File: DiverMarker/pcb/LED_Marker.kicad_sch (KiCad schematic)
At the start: 27 parts, among them IC101 PIC16LF15313, J101 SKEDD6, Q100 BST-52, Q101 BST-52, SW101 MK15-C2

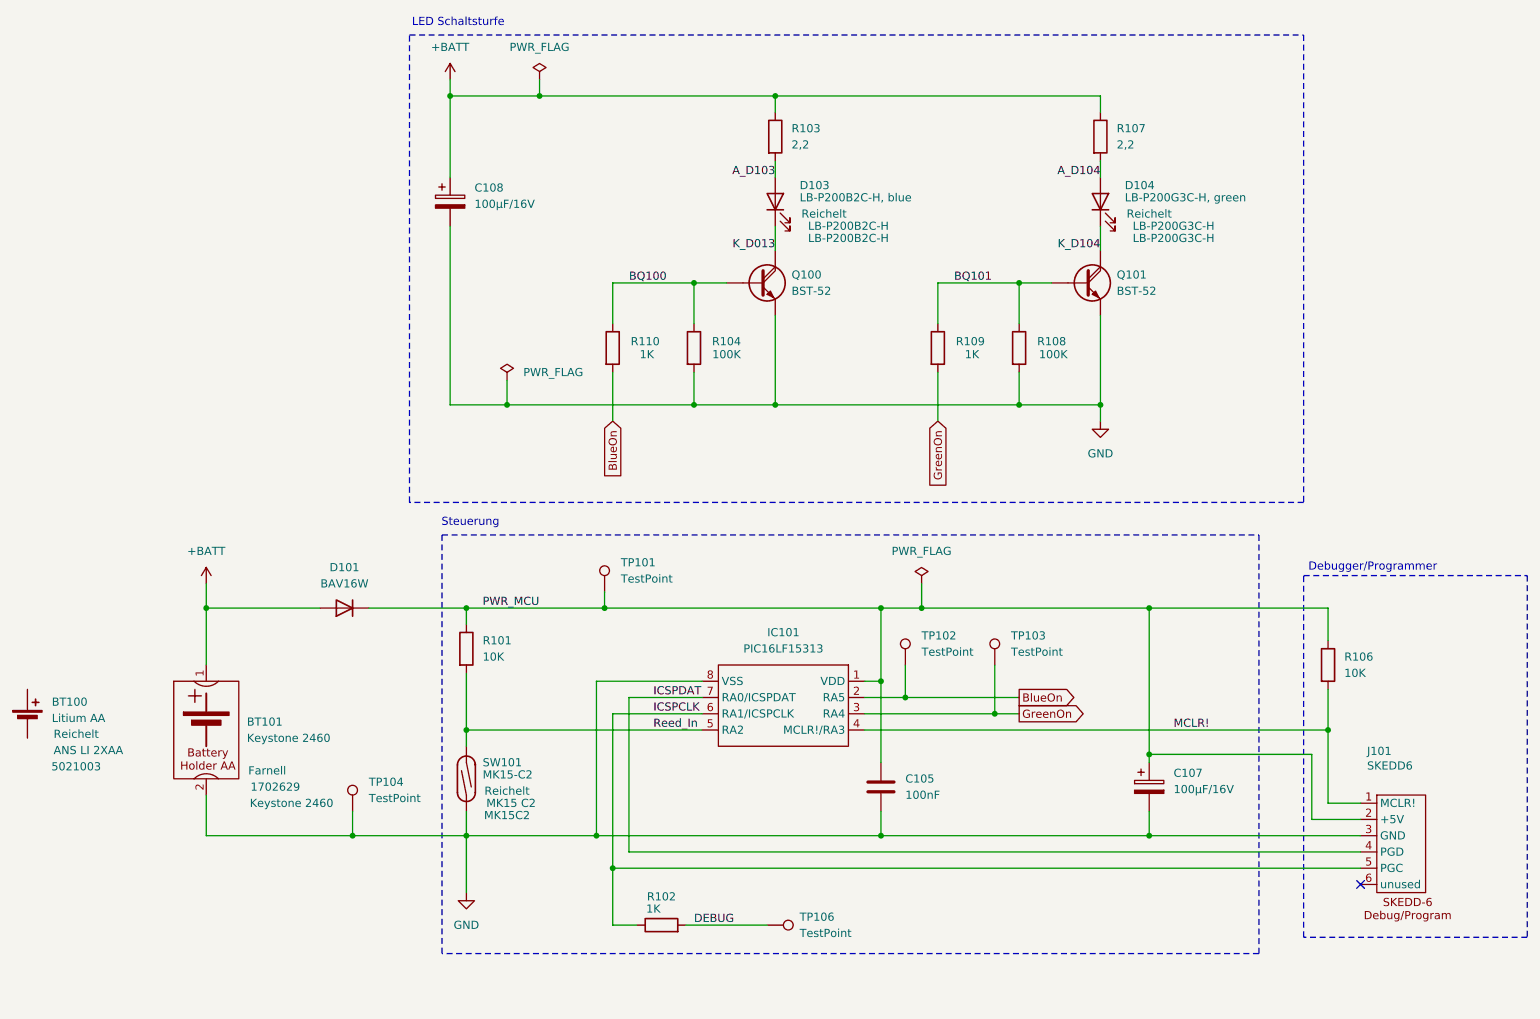
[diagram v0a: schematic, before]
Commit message: Distributors for all componentes added.
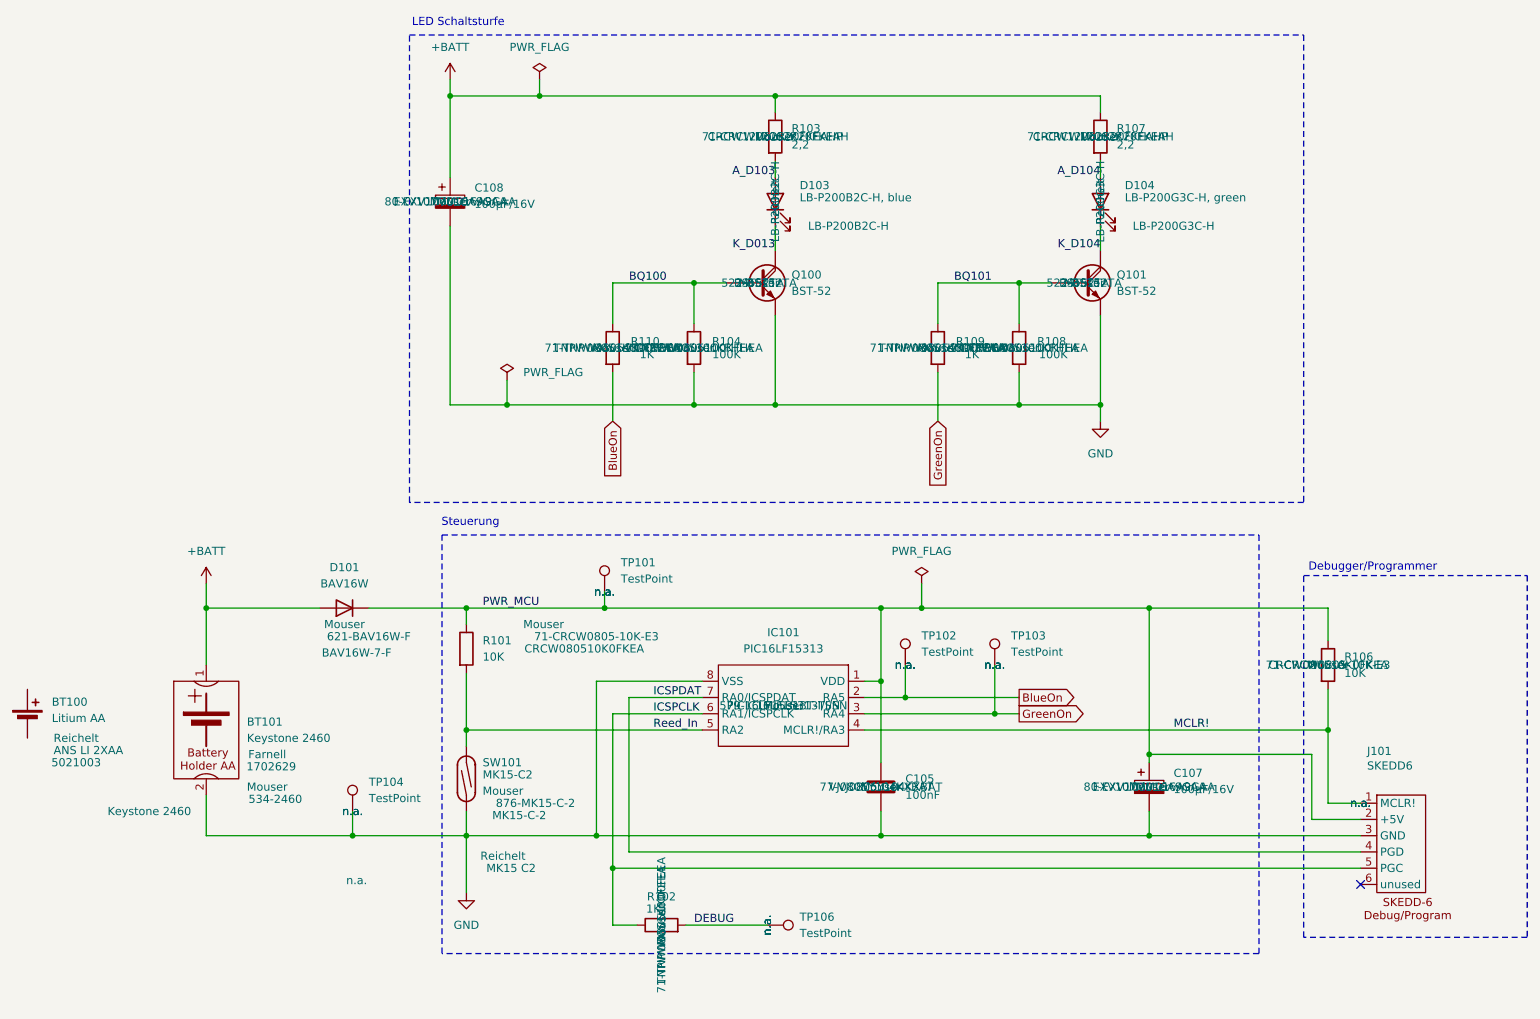
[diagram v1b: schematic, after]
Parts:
- BT100: footprint Battery:BatteryHolder_Keystone_2460_1xAA -> n.a.; Distr. Best.-Nr ANS LI 2XAA -> (none); Distr. Best.-Nr_1 (none) -> ANS LI 2XAA; Distributor Reichelt -> (none); Distributor_1 (none) -> Reichelt
- BT101: Distr. Best.-Nr 1702629 -> (none); Distr. Best.-Nr_1 (none) -> 534-2460; Distr. Best.-Nr_2 (none) -> 1702629; Distributor Farnell -> (none); Distributor_1 (none) -> Mouser; Distributor_2 (none) -> Farnell
- C105: Distr. Best.-Nr_1 (none) -> 77-VJ0805Y104KXBAT; Distributor_1 (none) -> Mouser; Herstellernummer (none) -> VJ0805Y104KXBAT
- C107, C108: Distr. Best.-Nr_1 (none) -> 80-EXV107M016A9GAA; Distributor_1 (none) -> Mouser; Herstellernummer (none) -> EXV107M016A9GAA
- D101: Distr. Best.-Nr_1 (none) -> 621-BAV16W-F; Distributor_1 (none) -> Mouser; Herstellernummer (none) -> BAV16W-7-F
- D103: Distr. Best.-Nr LB-P200B2C-H -> (none); Distr. Best.-Nr_1 (none) -> LB-P200B2C-H; Distributor Reichelt -> (none); Distributor_1 (none) -> Reichelt
- D104: Distr. Best.-Nr LB-P200G3C-H -> (none); Distr. Best.-Nr_1 (none) -> LB-P200G3C-H; Distributor Reichelt -> (none); Distributor_1 (none) -> Reichelt
- IC101: Distr. Best.-Nr_1 (none) -> 579-IC16LF15313TI/SN; Distributor_1 (none) -> Mouser; Herstellernummer (none) -> PIC16LF15313T-I/SN
- J101, TP101, TP102, TP103, TP104, TP106: Distr. Best.-Nr_1 (none) -> n.a.; Distributor_1 (none) -> n.a.; Herstellernummer (none) -> n.a.
- Q100, Q101: Distr. Best.-Nr_1 (none) -> 522-BST52TA; Distributor_1 (none) -> Mouser; Herstellernummer (none) -> BST52TA
- R101, R106: Distr. Best.-Nr_1 (none) -> 71-CRCW0805-10K-E3; Distributor_1 (none) -> Mouser; Herstellernummer (none) -> CRCW080510K0FKEA
- R102, R109, R110: Distr. Best.-Nr_1 (none) -> 71-TNPW08051K00FEEA; Distributor_1 (none) -> Mouser; Herstellernummer (none) -> TNPW08051K00FEEA
- R103, R107: Distr. Best.-Nr_1 (none) -> 71-CRCW12062R20FKEAH; Distributor_1 (none) -> Mouser; Herstellernummer (none) -> CRCW12062R20FKEAHP
- R104, R108: Distr. Best.-Nr_1 (none) -> 71-TNPW0805100KFHEA; Distributor_1 (none) -> Mouser; Herstellernummer (none) -> TNPW0805100KFHEA
- SW101: Distr. Best.-Nr MK15 C2 -> (none); Distr. Best.-Nr_1 (none) -> 876-MK15-C-2; Distr. Best.-Nr_2 (none) -> MK15 C2; Distributor Reichelt -> (none); Distributor_1 (none) -> Mouser; Distributor_2 (none) -> Reichelt; Herstellernummer MK15C2 -> MK15-C-2

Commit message: Working on BON
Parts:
- J101, TP101, TP102, TP103, TP104, TP106: Distributor_1 n.a. -> (none)
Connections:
- net GND: no longer C107.2, J101.3 (GND)
- new net: C107.2, J101.3 (GND)

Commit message: Minor changes: - LED blue replaced by red one (curret is on blue too low) - LED resistors changed from 2.2Ohm to 1Ohm - quiescent current added (about 25µA)
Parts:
- removed D103: LB-P200B2C-H, blue, MyLED:LPB200XX, symbol Device:LED
- added D105: LB-P200R1C-H, red, MyLED:LPB200XX, symbol Device:LED
- R103, R107: value 2,2 -> 1; Distr. Best.-Nr_1 71-CRCW12062R20FKEAH -> 71-CRCW12061R00FKEAH; Herstellernummer CRCW12062R20FKEAHP -> CRCW12061R00FKEAHP
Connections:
- net A_D103: now also D105.2 (A)
- net K_D013: now also D105.1 (K)

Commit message: Table with current measurements added.
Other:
- note added: "LED-Strom ca. 100mA"
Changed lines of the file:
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@@
 	)
 	(rectangle
-		(start 87.63 96.52)
-		(end 215.265 161.925)
+		(start 86.36 100.33)
+		(end 213.995 165.735)
 		(stroke
 			(width 0)
@@
 		)
 	)
+	(text "LED-Strom ca. 100mA"
+		(exclude_from_sim no)
+		(at 165.608 38.608 0)
+		(effects
+			(font
+				(size 1.27 1.27)
+			)
+		)
+	)
 	(text "LED Schaltsturfe\n"
 		(exclude_from_sim no)
@@
 		)
 	)
+	(table
+		(column_count 3)
+		(border
+			(external yes)
+			(header yes)
+			(stroke
+				(width 0)
+				(type solid)
+			)
+		)
+		(separators
+			(rows yes)
+			(cols yes)
+			(stroke
+				(width 0)
+				(type solid)
+			)
+		)
+		(column_widths 19.05 19.05 19.05)
+		(row_heights 2.54 2.54 2.54)
+		(cells
+			(table_cell ""
+				(exclude_from_sim no)
+				(at 226.06 17.78 0)
+				(size 19.05 2.54)
+				(margins 0.9525 0.9525 0.9525 0.9525)
+				(span 1 1)
+				(fill
+					(type none)
+				)
+				(effects
+					(font
+						(size 1.27 1.27)
+					)
+					(justify left top)
+				)
+			)
+			(table_cell "LED rot"
+				(exclude_from_sim no)
+				(at 245.11 17.78 0)
+				(size 19.05 2.54)
+				(margins 0.9525 0.9525 0.9525 0.9525)
+				(span 1 1)
+				(fill
+					(type none)
+				)
+				(effects
+					(font
+						(size 1.27 1.27)
+					)
+					(justify left top)
+				)
+			)
+			(table_cell "LED grün"
+				(exclude_from_sim no)
+				(at 264.16 17.78 0)
+				(size 19.05 2.54)
+				(margins 0.9525 0.9525 0.9525 0.9525)
+				(span 1 1)
+				(fill
+					(type none)
+				)
+				(effects
+					(font
+						(size 1.27 1.27)
+					)
+					(justify left top)
+				)
+			)
+			(table_cell "Brennspannung"
+				(exclude_from_sim no)
+				(at 226.06 20.32 0)
+				(size 19.05 2.54)
+				(margins 0.9525 0.9525 0.9525 0.9525)
+				(span 1 1)
+				(fill
+					(type none)
+				)
+				(effects
+					(font
+						(size 1.27 1.27)
+					)
+					(justify left top)
+				)
+			)
+			(table_cell "2,3V"
+				(exclude_from_sim no)
+				(at 245.11 20.32 0)
+				(size 19.05 2.54)
+				(margins 0.9525 0.9525 0.9525 0.9525)
+				(span 1 1)
+				(fill
+					(type none)
+				)
+				(effects
+					(font
+						(size 1.27 1.27)
+					)
+					(justify left top)
+				)
+			)
+			(table_cell "3,2V"
+				(exclude_from_sim no)
+				(at 264.16 20.32 0)
+				(size 19.05 2.54)
+				(margins 0.9525 0.9525 0.9525 0.9525)
+				(span 1 1)
+				(fill
+					(type none)
+				)
+				(effects
+					(font
+						(size 1.27 1.27)
+					)
+					(justify left top)
+				)
+			)
+			(table_cell "Strom @1Ohm"
+				(exclude_from_sim no)
+				(at 226.06 22.86 0)
+				(size 19.05 2.54)
+				(margins 0.9525 0.9525 0.9525 0.9525)
+				(span 1 1)
+				(fill
+					(type none)
+				)
+				(effects
+					(font
+						(size 1.27 1.27)
+					)
+					(justify left top)
+				)
+			)
+			(table_cell "122mA"
+				(exclude_from_sim no)
+				(at 245.11 22.86 0)
+				(size 19.05 2.54)
+				(margins 0.9525 0.9525 0.9525 0.9525)
+				(span 1 1)
+				(fill
+					(type none)
+				)
+				(effects
+					(font
+						(size 1.27 1.27)
+					)
+					(justify left top)
+				)
+			)
+			(table_cell "53mA"
+				(exclude_from_sim no)
+				(at 264.16 22.86 0)
+				(size 19.05 2.54)
+				(margins 0.9525 0.9525 0.9525 0.9525)
+				(span 1 1)
+				(fill
+					(type none)
+				)
+				(effects
+					(font
+						(size 1.27 1.27)
+					)
+					(justify left top)
+				)
+			)
+		)
+	)
